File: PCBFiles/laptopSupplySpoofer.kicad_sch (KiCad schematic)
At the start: 4 parts, among them J1 Screw_Terminal_01x02, J2 Screw_Terminal_01x03, U1 DS2431

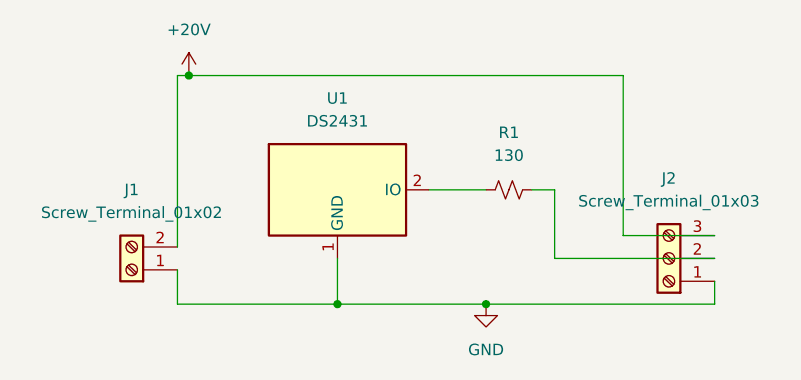
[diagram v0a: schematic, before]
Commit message: removed delay_us source files and integrated it into ds2431.c for a more clean build also updated PCB files
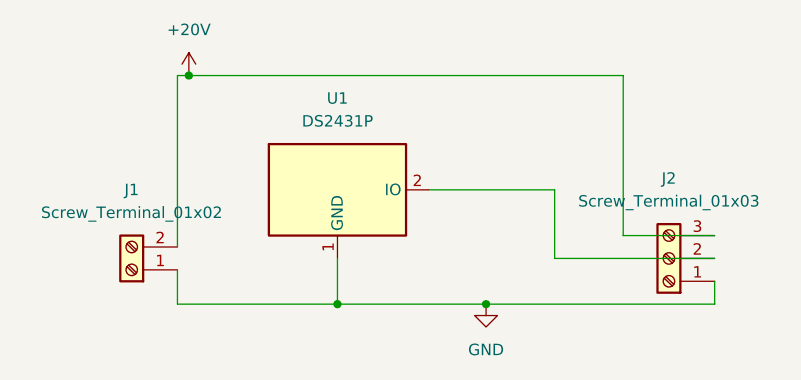
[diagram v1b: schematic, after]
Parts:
- removed R1: 130, Resistor_THT:R_Axial_DIN0207_L6.3mm_D2.5mm_P7.62mm_Horizontal, symbol Device:R_Small_US
- removed U1: DS2431, Package_TO_SOT_THT:TO-92_Inline, symbol Memory_EEPROM:DS2431
- added U1: DS2431P, Package_SO_J-Lead:TSOC-6_3.76x3.94mm_P1.27mm, symbol Memory_EEPROM:DS2431P
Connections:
- net GND: now also U1.1 (GND)
- net at J2.2 (Pin_2): now also U1.2 (IO)
- new net: U1.3 (NC), U1.4 (NC), U1.5 (NC), U1.6 (NC)
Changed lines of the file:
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@@
 	(wire
 		(pts
-			(xy 118.11 73.66) (xy 124.46 73.66)
+			(xy 118.11 73.66) (xy 132.08 73.66)
 		)
 		(stroke
@@
 		(pts
 			(xy 107.95 81.28) (xy 107.95 86.36)
-		)
-		(stroke
-			(width 0)
-			(type default)
-		)
-	)
-	(wire
-		(pts
-			(xy 129.54 73.66) (xy 132.08 73.66)
 		)
 		(stroke
@@
 			(width 0)
 			(type default)
-		)
-	)
-	(symbol
-		(lib_id "Device:R_Small_US")
-		(at 127 73.66 270)
-		(unit 1)
-		(exclude_from_sim no)
-		(in_bom yes)
-		(on_board yes)
-		(dnp no)
-		(fields_autoplaced yes)
-		(property "Reference" "R1"
-			(at 127 67.31 90)
-			(effects
-				(font
-					(size 1.27 1.27)
-				)
-			)
-		)
-		(property "Value" "130"
-			(at 127 69.85 90)
-			(effects
-				(font
-					(size 1.27 1.27)
-				)
-			)
-		)
-		(property "Footprint" "Resistor_THT:R_Axial_DIN0207_L6.3mm_D2.5mm_P7.62mm_Horizontal"
-			(at 127 73.66 0)
-			(effects
-				(font
-					(size 1.27 1.27)
-				)
-				(hide yes)
-			)
-		)
-		(property "Datasheet" "~"
-			(at 127 73.66 0)
-			(effects
-				(font
-					(size 1.27 1.27)
-				)
-				(hide yes)
-			)
-		)
-		(property "Description" "Resistor, small US symbol"
-			(at 127 73.66 0)
-			(effects
-				(font
-					(size 1.27 1.27)
-				)
-				(hide yes)
-			)
-		)
-		(pin "1"
-		)
-		(pin "2"
-		)
-		(instances
-			(project ""
-				(path "/1c7e6398-1e52-4c78-9b8c-ef1e64772bc1"
-					(reference "R1")
-					(unit 1)
-				)
-			)
 		)
 	)
@@
 	)
 	(symbol
-		(lib_id "Memory_EEPROM:DS2431")
+		(lib_id "Memory_EEPROM:DS2431P")
 		(at 107.95 73.66 0)
 		(unit 1)
@@
 			)
 		)
-		(property "Value" "DS2431"
+		(property "Value" "DS2431P"
 			(at 107.95 66.04 0)
 			(effects
@@
 			)
 		)
-		(property "Footprint" "Package_TO_SOT_THT:TO-92_Inline"
+		(property "Footprint" "Package_SO_J-Lead:TSOC-6_3.76x3.94mm_P1.27mm"
 			(at 107.95 63.5 0)
 			(effects
@@
 			)
 		)
-		(property "Description" "1024-bit, 1-Wire® EEPROM chip, TO-92"
+		(property "Description" "1024-bit, 1-Wire® EEPROM chip, TSOC-6"
 			(at 107.95 58.42 0)
 			(effects
@@
 			)
 		)
-		(pin "1"
+		(pin "6"
+		)
+		(pin "5"
+		)
+		(pin "4"
 		)
 		(pin "2"
 		)
+		(pin "1"
+		)
 		(pin "3"
